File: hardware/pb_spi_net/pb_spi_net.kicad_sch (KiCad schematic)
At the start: 5 parts, among them J1 SPI, J2 ENC28J60 Module, J3 AirLift, U1 WIZ820IO

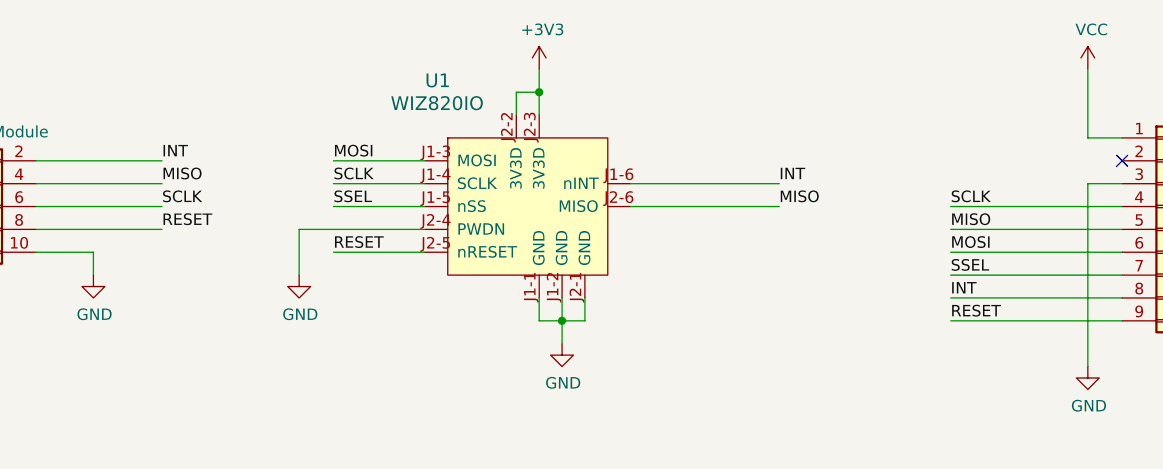
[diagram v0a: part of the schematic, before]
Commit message: fixed enc28j60 test
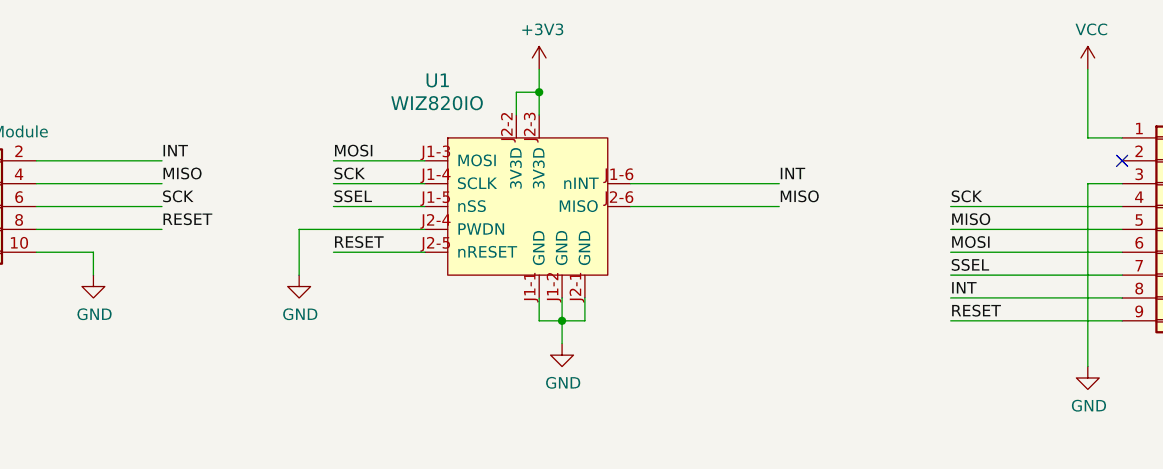
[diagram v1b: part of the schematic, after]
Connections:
- net SCLK is gone; now on net SCK: J2.6 (Pin_6), J3.4 (Pin_4), U1.J1-4 (SCLK)
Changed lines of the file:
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@@
     (effects (font (size 1.27 1.27)) (justify left bottom))
   )
-  (label "SCLK" (at 146.05 91.44 0)
+  (label "SCK" (at 146.05 91.44 0)
     (effects (font (size 1.27 1.27)) (justify left bottom))
   )
@@
     (effects (font (size 1.27 1.27)) (justify left bottom))
   )
-  (label "SCLK" (at 165.1 88.9 0)
+  (label "SCK" (at 165.1 88.9 0)
     (effects (font (size 1.27 1.27)) (justify left bottom))
   )
@@
     (effects (font (size 1.27 1.27)) (justify left bottom))
   )
-  (label "SCLK" (at 233.68 91.44 0)
+  (label "SCK" (at 233.68 91.44 0)
     (effects (font (size 1.27 1.27)) (justify left bottom))
   )
